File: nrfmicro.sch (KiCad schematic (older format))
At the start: 24 parts, among them J1 USB_OTG, J2 Serial Connector, J3 Conn_01x02, J4 USB_C_Receptacle_USB2.0, Q1 DMG2305, SW1 SW_SPDT, U2 ProMicro, U3 AP2112K-3.3, U4 MCP73831-2-OT, U5 E73-2G4M08S1C-52840, Y2 32,768

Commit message: second commit
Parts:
- renumbered C9 to C3, C5 to C4, C6 to C5, D3 to D2, J4 to J2, J2 to J3, J3 to J4, R3 to R1, R4 to R2, R2 to R3, R5 to R4
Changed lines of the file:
@@
 U 1 1 5B158495
 P 1400 6850
-F 0 "D1" H 1400 6950 50  0000 C CNN
-F 1 "MBR120" H 1400 6750 50  0000 C CNN
+F 0 "D1" H 1400 6634 50  0000 C CNN
+F 1 "MBR120" H 1400 6725 50  0000 C CNN
 F 2 "Diode_SMD:D_SOD-123F" H 1400 6675 50  0001 C CNN
 F 3 "" H 1400 6850 50  0001 C CNN
@@
 $EndComp
 $Comp
-L nrfmicro-rescue:C C5
+L nrfmicro-rescue:C C4
 U 1 1 5B158BD8
 P 1700 7200
-F 0 "C5" H 1725 7300 50  0000 L CNN
+F 0 "C4" H 1725 7300 50  0000 L CNN
 F 1 "10uF" H 1725 7100 50  0000 L CNN
 F 2 "Capacitor_SMD:C_0805_2012Metric" H 1738 7050 50  0001 C CNN
@@
 	3850 6850 3850 6700
 $Comp
-L nrfmicro-rescue:R R2
+L nrfmicro-rescue:R R3
 U 1 1 5B159927
 P 1050 7200
-F 0 "R2" H 1120 7246 50  0000 L CNN
+F 0 "R3" H 1120 7246 50  0000 L CNN
 F 1 "100K" H 1120 7155 50  0000 L CNN
 F 2 "Resistor_SMD:R_0805_2012Metric" V 980 7200 50  0001 C CNN
@@
 LiPo Charging\n
 $Comp
-L nrfmicro-rescue:Conn_01x02 J3
+L nrfmicro-rescue:Conn_01x02 J4
 U 1 1 5B15B915
 P 10850 2100
-F 0 "J3" H 10769 2317 50  0000 C CNN
+F 0 "J4" H 10769 2317 50  0000 C CNN
 F 1 "Conn_01x02" H 10769 2226 50  0000 C CNN
 F 2 "nrfmicro:battery_holder_bs-7" H 10850 2100 50  0001 C CNN
@@
 	1050 6850 1050 7050
 $Comp
-L Connector:USB_C_Receptacle_USB2.0 J4
+L Connector:USB_C_Receptacle_USB2.0 J2
 U 1 1 5C71F6FD
 P 8500 2650
-F 0 "J4" H 8605 3517 50  0000 C CNN
+F 0 "J2" H 8605 3517 50  0000 C CNN
 F 1 "USB_C_Receptacle_USB2.0" H 8605 3426 50  0000 C CNN
 F 2 "nrfmicro:usb_type_c" H 8650 2650 50  0001 C CNN
@@
 $EndComp
 $Comp
-L Device:LED D3
+L Device:LED D2
 U 1 1 5C7015F2
 P 1500 5150
-F 0 "D3" H 1492 4895 50  0000 C CNN
+F 0 "D2" H 1492 4895 50  0000 C CNN
 F 1 "LED" H 1492 4986 50  0000 C CNN
 F 2 "LED_SMD:LED_0603_1608Metric" H 1500 5150 50  0001 C CNN
@@
 $EndComp
 $Comp
-L Device:R R3
+L Device:R R1
 U 1 1 5C7015F9
 P 1850 5150
-F 0 "R3" V 2057 5150 50  0000 C CNN
+F 0 "R1" V 2057 5150 50  0000 C CNN
 F 1 "1K" V 1966 5150 50  0000 C CNN
 F 2 "Resistor_SMD:R_0805_2012Metric" V 1780 5150 50  0001 C CNN
@@
 $EndComp
 $Comp
-L Device:C C9
+L Device:C C3
 U 1 1 5C70161B
 P 3600 5150
-F 0 "C9" H 3715 5196 50  0000 L CNN
+F 0 "C3" H 3715 5196 50  0000 L CNN
 F 1 "10uF" H 3715 5105 50  0000 L CNN
 F 2 "Capacitor_SMD:C_0805_2012Metric" H 3638 5000 50  0001 C CNN
@@
 $EndComp
 $Comp
-L Device:R R4
+L Device:R R2
 U 1 1 5C701629
 P 3150 5150
-F 0 "R4" V 3357 5150 50  0000 C CNN
+F 0 "R2" V 3357 5150 50  0000 C CNN
 F 1 "4.7K" V 3266 5150 50  0000 C CNN
 F 2 "Resistor_SMD:R_0805_2012Metric" V 3080 5150 50  0001 C CNN
@@
 $EndComp
 $Comp
-L nrfmicro-rescue:R R5
+L nrfmicro-rescue:R R4
 U 1 1 5CC730D9
 P 2350 7100
-F 0 "R5" H 2281 7146 50  0000 R CNN
+F 0 "R4" H 2281 7146 50  0000 R CNN
 F 1 "100K" H 2281 7055 50  0000 R CNN
 F 2 "Resistor_SMD:R_0805_2012Metric" V 2280 7100 50  0001 C CNN
@@
 	2350 6850 2550 6850
 $Comp
-L nrfmicro-rescue:C C6
+L nrfmicro-rescue:C C5
 U 1 1 5CC9355F
 P 3850 7200
-F 0 "C6" H 3875 7300 50  0000 L CNN
+F 0 "C5" H 3875 7300 50  0000 L CNN
 F 1 "10uF" H 3875 7100 50  0000 L CNN
 F 2 "Capacitor_SMD:C_0805_2012Metric" H 3888 7050 50  0001 C CNN
@@
 	3850 7350 3850 7400
 $Comp
-L Connector_Generic:Conn_01x04 J2
+L Connector_Generic:Conn_01x04 J3
 U 1 1 5AC0089B
 P 9850 1150
-F 0 "J2" H 9850 1450 50  0000 C CNN
+F 0 "J3" H 9850 1450 50  0000 C CNN
 F 1 "Serial Connector" H 9600 700 50  0000 C CNN
 F 2 "nrfmicro:connector_swd" H 9850 1150 50  0001 C CNN

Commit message: pushed to version 0.2
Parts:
- added D3: LED, LED_SMD:LED_0603_1608Metric, symbol Device:LED
- added R5: 1K, Resistor_SMD:R_0603_1608Metric, symbol Device:R
- R1: footprint Resistor_SMD:R_0805_2012Metric -> Resistor_SMD:R_0603_1608Metric
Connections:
- net labels added: BLUE_LED, DFU
- net labels removed: LED2, MISO, MOSI, SCK, SCL, SDA
- wire segments 118 -> 106
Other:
- note added: "1.0"
- note added: "Feather pins:\n\nP1.15 LED1 x\nP1.10 LED2\nP0.15 BTN1\nP0.19 BTN2 x\nP0.16 NEOPIXEL x\nP0.08 RX\nP0.06 TX\n\nP1.02 DFU\nP0.18 RESET\n"
- note added: "Feb24, 2019"
- note added: "nrfmicro"
- note removed: "2.0"
- note removed: "BlueMicro V2.0"
- note removed: "Feather pins:\n\nP1.15 LED1 x\nP1.10 LED2\nP0.15 BTN1\nP0.19 BTN2 x\nP0.16 NEOPIXEL x\nP0.08 RX\nP0.06 TX\n"
- note removed: "June 18, 2018"
- moved on the sheet: JP1, SW1
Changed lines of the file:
@@
 	5300 1200 5350 1200
 Connection ~ 5300 1150
-Wire Wire Line
-	6350 1300 6550 1300
-Wire Wire Line
-	6350 1400 6550 1400
-Wire Wire Line
-	6350 1500 6550 1500
-Wire Wire Line
-	6350 1600 6550 1600
 Text Label 6350 1300 0    60   ~ 0
+P0.30
+Text Label 6350 1400 0    60   ~ 0
 P0.31
-Text Label 6350 1400 0    60   ~ 0
+Text Label 6350 1500 0    60   ~ 0
 P0.29
-Text Label 6350 1500 0    60   ~ 0
+Text Label 6350 1600 0    60   ~ 0
 P0.02
-Text Label 6350 1600 0    60   ~ 0
-P1.13
-Wire Wire Line
-	5350 1500 5150 1500
 Text Label 6350 2000 0    60   ~ 0
 P1.11
-Text Label 5150 1500 0    60   ~ 0
-P1.00
+Text Label 5350 1500 2    60   ~ 0
+P0.20
 $Comp
 L nrfmicro-rescue:USB_OTG J1
@@
 Connection ~ 1050 6500
 Wire Wire Line
-	2000 6300 2000 6250
-Wire Wire Line
 	3150 6850 3850 6850
 $Comp
@@
 Wire Notes Line
 	4500 5950 4500 7800
-Text Notes 2650 6250 0    60   ~ 0
+Text Notes 3350 6200 0    60   ~ 0
 Power and Filtering
 Wire Wire Line
@@
 NoConn ~ 8200 1450
 Text Notes 7550 7500 0    60   ~ 0
-BlueMicro V2.0
+nrfmicro
 Text Notes 8250 7650 0    60   ~ 0
-June 18, 2018
+Feb24, 2019
 Text Notes 10650 7650 0    60   ~ 0
-2.0
+1.0
 Wire Wire Line
 	5300 1150 5300 1200
@@
 F 0 "R1" V 2057 5150 50  0000 C CNN
 F 1 "1K" V 1966 5150 50  0000 C CNN
-F 2 "Resistor_SMD:R_0805_2012Metric" V 1780 5150 50  0001 C CNN
+F 2 "Resistor_SMD:R_0603_1608Metric" V 1780 5150 50  0001 C CNN
 F 3 "~" H 1850 5150 50  0001 C CNN
 	1    1850 5150
@@
 Text GLabel 950  6250 0    60   Input ~ 0
 VBUS
-Text GLabel 1900 6250 0    60   Input ~ 0
+Text GLabel 3000 6350 2    60   Input ~ 0
 VBAT
-Text Label 5150 2000 0    60   ~ 0
+Text Label 5350 2000 2    60   ~ 0
+P1.06
+Text Label 5350 1900 2    60   ~ 0
 P0.10
-Text Label 5150 1900 0    60   ~ 0
-P1.06
-Text Label 5150 1800 0    60   ~ 0
+Text Label 5350 1800 2    60   ~ 0
 P0.09
-Text Label 5150 1700 0    60   ~ 0
-P1.04
-Text Label 5150 1600 0    60   ~ 0
-P1.02
-Wire Wire Line
-	5350 2000 5150 2000
-Wire Wire Line
-	5350 1900 5150 1900
-Wire Wire Line
-	5350 1800 5150 1800
-Wire Wire Line
-	5350 1700 5150 1700
-Wire Wire Line
-	5350 1600 5150 1600
+Text Label 5350 1700 2    60   ~ 0
+P0.24
+Text Label 5350 1600 2    60   ~ 0
+P0.13
 Text Label 1650 2550 2    60   ~ 0
 P0.08
@@
 Text Label 1650 1350 2    60   ~ 0
 P0.28
-Text GLabel 10000 2000 0    60   Input ~ 0
+Text GLabel 10400 2100 0    60   Input ~ 0
 VBAT
 Wire Wire Line
@@
 Wire Wire Line
 	2550 5550 1300 5550
-Wire Wire Line
-	6350 1900 6650 1900
-Wire Wire Line
-	6350 1700 6650 1700
-Wire Wire Line
-	6650 1800 6350 1800
 Text GLabel 5050 1000 0    60   Input ~ 0
 RXD
@@
 Wire Wire Line
 	5050 900  5350 900
-Wire Wire Line
-	5050 1300 5350 1300
-Wire Wire Line
-	5050 1400 5350 1400
-Text GLabel 5050 1400 0    60   Input ~ 0
-SCL
-Text GLabel 5050 1300 0    60   Input ~ 0
-SDA
-Text Label 5150 1300 0    60   ~ 0
-P0.22
-Text Label 5150 1400 0    60   ~ 0
-P0.24
+Text Label 5350 1300 2    60   ~ 0
+P0.15
+Text Label 5350 1400 2    60   ~ 0
+P0.17
 Text Label 6350 1700 0    60   ~ 0
+P1.13
+Text Label 6350 1900 0    60   ~ 0
 P0.28
-Text Label 6350 1900 0    60   ~ 0
-P1.10
 Text Label 6350 1800 0    60   ~ 0
 P0.03
-Text GLabel 3750 2450 2    60   Input ~ 0
+Text GLabel 3300 1850 2    60   Input ~ 0
 SWO
 Wire Wire Line
@@
 Existing pins:\n\nP0.02 P0.03 P0.04 P0.05 P0.06 P0.07 P0.08 P0.09\nP0.10 P0.12 P0.13 P0.15 P0.17 P0.18\nP0.20 P0.22 P0.24 P0.26 P0.28 P0.29\nP0.30 P0.31\n\nP1.00 P1.02 P1.04 P1.06 P1.09\nP1.10 P1.11 P1.13\n\n
 Text Notes 6750 3250 0    60   ~ 0
-Feather pins:\n\nP1.15 LED1 x\nP1.10 LED2\nP0.15 BTN1\nP0.19 BTN2 x\nP0.16 NEOPIXEL x\nP0.08 RX\nP0.06 TX\n
-Text GLabel 6650 1800 2    60   Input ~ 0
-MISO
-Text GLabel 6650 1700 2    60   Input ~ 0
-SCK
-Text GLabel 6650 1900 2    60   Input ~ 0
-MOSI
+Feather pins:\n\nP1.15 LED1 x\nP1.10 LED2\nP0.15 BTN1\nP0.19 BTN2 x\nP0.16 NEOPIXEL x\nP0.08 RX\nP0.06 TX\n\nP1.02 DFU\nP0.18 RESET\n
 Text Label 3000 1650 0    60   ~ 0
 P1.02
 Wire Wire Line
-	3000 2450 3750 2450
+	3000 1850 3300 1850
 Text GLabel 1300 1150 0    60   Input ~ 0
-LED2
+BLUE_LED
 Wire Wire Line
 	1650 1150 1300 1150
@@
 Wire Wire Line
 	950  6250 1050 6250
-Wire Wire Line
-	1900 6250 2000 6250
 Wire Wire Line
 	3850 7350 3850 7400
@@
 L Switch:SW_SPDT SW1
 U 1 1 5CB2FC09
-P 10200 2000
-F 0 "SW1" H 10200 2285 50  0000 C CNN
-F 1 "SW_SPDT" H 10200 2194 50  0000 C CNN
-F 2 "nrfmicro:switch_MSK-12C02_smd" H 10200 2000 50  0001 C CNN
-F 3 "" H 10200 2000 50  0001 C CNN
-	1    10200 2000
-	1    0    0    -1
-$EndComp
-NoConn ~ 10400 1900
+P 2800 6350
+F 0 "SW1" H 2800 6650 50  0000 C CNN
+F 1 "SW_SPDT" H 2800 6550 50  0000 C CNN
+F 2 "nrfmicro:switch_MSK-12C02_smd" H 2800 6350 50  0001 C CNN
+F 3 "" H 2800 6350 50  0001 C CNN
+	1    2800 6350
+	-1   0    0    -1
+$EndComp
+Text GLabel 3300 1650 2    60   Input ~ 0
+DFU
+Wire Wire Line
+	3000 1650 3300 1650
+Text GLabel 2700 4100 0    60   Input ~ 0
+BLUE_LED
+$Comp
+L Device:R R5
+U 1 1 5C73A719
+P 3150 4100
+F 0 "R5" V 3357 4100 50  0000 C CNN
+F 1 "1K" V 3266 4100 50  0000 C CNN
+F 2 "Resistor_SMD:R_0603_1608Metric" V 3080 4100 50  0001 C CNN
+F 3 "~" H 3150 4100 50  0001 C CNN
+	1    3150 4100
+	0    -1   -1   0
+$EndComp
+$Comp
+L power:GND #PWR0111
+U 1 1 5C73ECD6
+P 3300 4100
+F 0 "#PWR0111" H 3300 3850 50  0001 C CNN
+F 1 "GND" H 3305 3927 50  0000 C CNN
+F 2 "" H 3300 4100 50  0001 C CNN
+F 3 "" H 3300 4100 50  0001 C CNN
+	1    3300 4100
+	0    -1   -1   0
+$EndComp
+$Comp
+L Device:LED D3
+U 1 1 5C7545DA
+P 2850 4100
+F 0 "D3" H 2842 3845 50  0000 C CNN
+F 1 "LED" H 2842 3936 50  0000 C CNN
+F 2 "LED_SMD:LED_0603_1608Metric" H 2850 4100 50  0001 C CNN
+F 3 "~" H 2850 4100 50  0001 C CNN
+	1    2850 4100
+	-1   0    0    1
+$EndComp
 $Comp
 L Jumper:SolderJumper_2_Open JP1
 U 1 1 5C72844F
-P 4400 2100
-F 0 "JP1" H 4400 2305 50  0000 C CNN
-F 1 "SolderJumper_2_Open" H 4400 2214 50  0000 C CNN
-F 2 "nrfmicro:jumper" H 4400 2100 50  0001 C CNN
-F 3 "~" H 4400 2100 50  0001 C CNN
-	1    4400 2100
+P 1500 4100
+F 0 "JP1" H 1500 4305 50  0000 C CNN
+F 1 "SolderJumper_2_Open" H 1500 4214 50  0000 C CNN
+F 2 "nrfmicro:jumper" H 1500 4100 50  0001 C CNN
+F 3 "~" H 1500 4100 50  0001 C CNN
+	1    1500 4100
 	1    0    0    -1
 $EndComp
@@
 L power:GND #PWR0110
 U 1 1 5C72CA36
-P 4550 2100
-F 0 "#PWR0110" H 4550 1850 50  0001 C CNN
-F 1 "GND" H 4555 1927 50  0000 C CNN
-F 2 "" H 4550 2100 50  0001 C CNN
-F 3 "" H 4550 2100 50  0001 C CNN
-	1    4550 2100
+P 1650 4100
+F 0 "#PWR0110" H 1650 3850 50  0001 C CNN
+F 1 "GND" H 1655 3927 50  0000 C CNN
+F 2 "" H 1650 4100 50  0001 C CNN
+F 3 "" H 1650 4100 50  0001 C CNN
+	1    1650 4100
 	0    -1   -1   0
 $EndComp
-Text Label 4250 2100 2    60   ~ 0
-P0.26
+Text GLabel 1350 4100 0    60   Input ~ 0
+DFU
+NoConn ~ 2600 6250
+Wire Wire Line
+	2000 6300 2000 6250
+Wire Wire Line
+	2000 6250 2500 6250
+Wire Wire Line
+	2500 6250 2500 6450
+Wire Wire Line
+	2500 6450 2600 6450
 $EndSCHEMATC

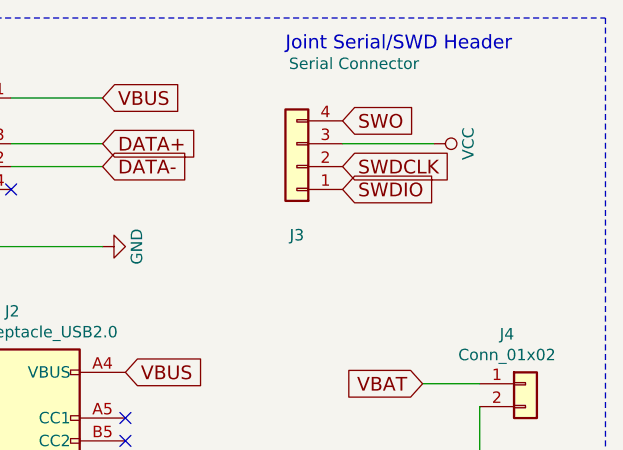
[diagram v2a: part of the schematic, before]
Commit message: fixed SWDCLK typo, fully autorouted and optimized
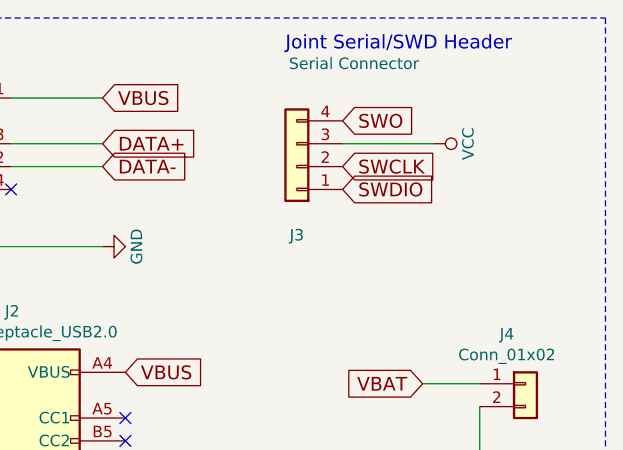
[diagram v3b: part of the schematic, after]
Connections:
- net SWDCLK is gone; now on net SWCLK: J3.2 (Pin_2)
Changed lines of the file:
@@
 	11200 500  11200 6500
 Text GLabel 10050 1150 2    60   Input ~ 0
-SWDCLK
+SWCLK
 Text GLabel 10050 1250 2    60   Input ~ 0
 SWDIO
